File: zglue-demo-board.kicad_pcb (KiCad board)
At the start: 6 copper layers, 56 x 66 mm, 151 parts, among them J1 3220-10-0100-00, J10 0473460001, J2 DF13A-2P-1.25H, J3 3220-10-0100-00, J4 2x20_Header_Female, J5 0473460001, J6 556500488, J7 556500488, J8 WE_686115148922, J9 WE_686115148922_FLIPPED, U1 MCP1700T-3302E_TT, U2 NTS0104BQ, U3 NTS0104BQ, U4 NTS0104BQ, U5 93LC56CT-IMC, U6 FT4232HQ, U7 NTB0104BQ, U8 NTB0104BQ, Y1 ASFLMB-12.000MHZ-LC-T

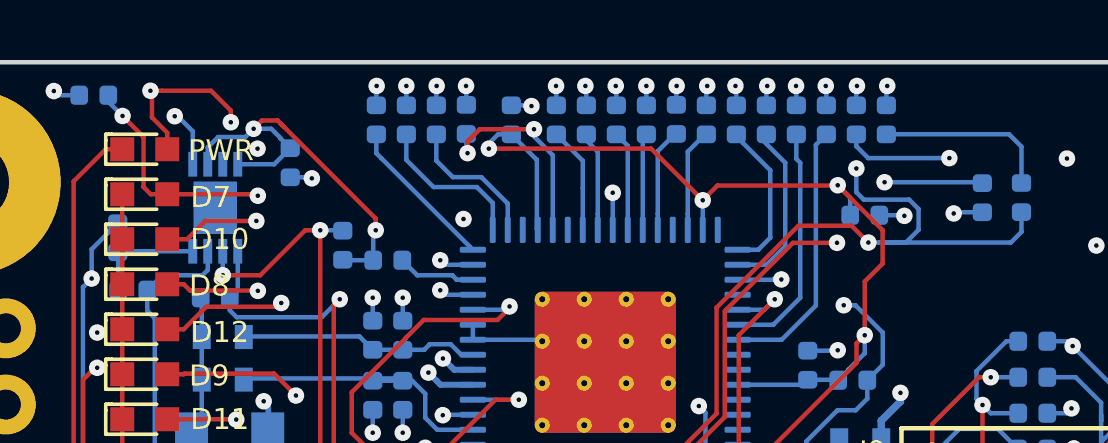
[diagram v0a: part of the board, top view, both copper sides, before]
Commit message: Layout components moved away from PCB edges
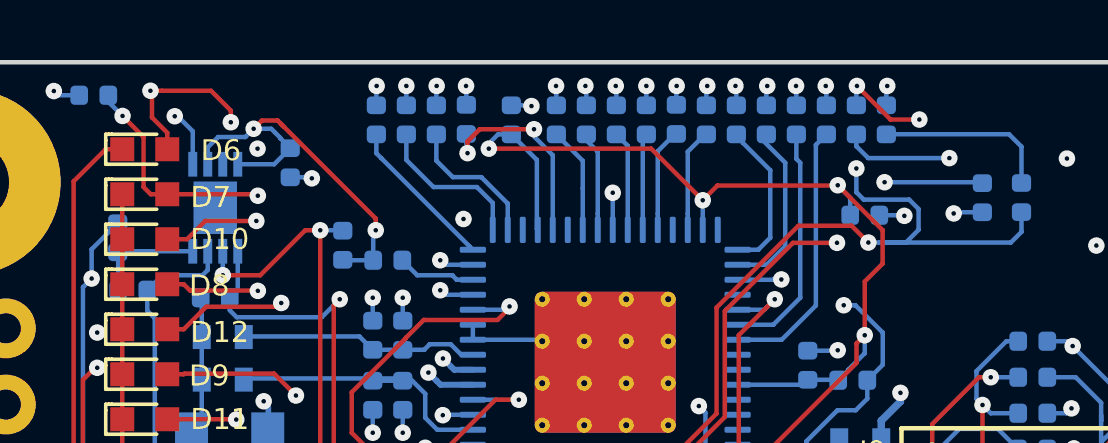
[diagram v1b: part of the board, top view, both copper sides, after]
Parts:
- C1, C2, C3, C4, C5: footprint antmicro-footprints:0603-cap -> zglue-demo-board-footprints:0603-cap
- C10, C11, C12, C13, C14, C15, C16, C17, C18, C19, C20, C21, C22, C23, C24, C25, C26, C9: footprint antmicro-footprints:0402-cap -> zglue-demo-board-footprints:0402-cap
- D1, D3, D4: footprint antmicro-footprints:SOD-123 -> zglue-demo-board-footprints:SOD-123
- D10, D11, D12, D13, D7, D8, D9: footprint antmicro-footprints:LED_0603 -> zglue-demo-board-footprints:LED_0603
- D2, D5: footprint antmicro-footprints:SOT-3 -> zglue-demo-board-footprints:SOT-3
- D6: renamed from PWR; footprint antmicro-footprints:LED_0603 -> zglue-demo-board-footprints:LED_0603
- FB1, FB2, R1: footprint antmicro-footprints:0603-res -> zglue-demo-board-footprints:0603-res
- J1, J3: footprint antmicro-footprints:PinHeader_2x5_P1.27mm_Drill.7mm -> zglue-demo-board-footprints:PinHeader_2x5_P1.27mm_Drill.7mm
- J10, J5: footprint antmicro-footprints:USB_Micro_B_Female_0473460001 -> zglue-demo-board-footprints:USB_Micro_B_Female_0473460001
- J2: footprint antmicro-footprints:DF13A-2P-1.25H -> zglue-demo-board-footprints:DF13A-2P-1.25H
- J4: footprint antmicro-footprints:PinHeader_2x40_P2.54_Drill1mm -> zglue-demo-board-footprints:PinHeader_2x40_P2.54_Drill1mm
- J6, J7: footprint antmicro-footprints:556500488 -> zglue-demo-board-footprints:556500488
- J8: footprint antmicro-footprints:WE_686115148922 -> zglue-demo-board-footprints:WE_686115148922
- J9: footprint antmicro-footprints:WE_686115148922_FLIPPED -> zglue-demo-board-footprints:WE_686115148922_FLIPPED
- N1: footprint antmicro-footprints:antmicro-logo_scaled_20mm -> zglue-demo-board-footprints:antmicro-logo_scaled_20mm
- N2: footprint antmicro-footprints:zglue-logo-10000dpi -> zglue-demo-board-footprints:zglue-logo-10000dpi
- N2: footprint antmicro-footprints:zglue-logo -> zglue-demo-board-footprints:zglue-logo
- N3: footprint antmicro-footprints:oshw-logo -> zglue-demo-board-footprints:oshw-logo
- R10, R11, R12, R13, R14, R15, R16, R17, R18, R19, R2, R20, R21, R22, R23, R24, R25, R26, R27, R28, R29, R3, R30, R31, R32, R33, R34, R35, R36, R37, R38, R39, R4, R40, R41, R42, R43, R44, R45, R46, R47, R48, R49, R5, R50, R51, R52, R53, R54, R55, R56, R57, R58, R59, R6, R7, R8, R9: footprint antmicro-footprints:0402-res -> zglue-demo-board-footprints:0402-res
- REF** (x4): footprint antmicro-footprints:Mount-hole-M2.5 -> zglue-demo-board-footprints:Mount-hole-M2.5
- S1: footprint antmicro-footprints:Panasonic_EVQPUJ_EVQPUA -> zglue-demo-board-footprints:Panasonic_EVQPUJ_EVQPUA
- TP1, TP10, TP11, TP12, TP13, TP14, TP15, TP16, TP17, TP18, TP19, TP2, TP20, TP21, TP22, TP23, TP3, TP4, TP5, TP6, TP7, TP8, TP9: footprint antmicro-footprints:Testpoint_smd_1mm -> zglue-demo-board-footprints:Testpoint_smd_1mm
- U1: footprint antmicro-footprints:SOT-23-3 -> zglue-demo-board-footprints:SOT-23-3
- U2, U3, U4, U7, U8: footprint antmicro-footprints:QDHVQFN14 -> zglue-demo-board-footprints:QDHVQFN14
- U5: footprint antmicro-footprints:DFN-8_2x3mm -> zglue-demo-board-footprints:DFN-8_2x3mm
- U6: footprint antmicro-footprints:FT4232HQ -> zglue-demo-board-footprints:FT4232HQ
- Y1: footprint antmicro-footprints:ASFLMB -> zglue-demo-board-footprints:ASFLMB
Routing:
- net Net-(J4-Pad8): track 77.4 -> 81.3 mm, vias 1 -> 2
